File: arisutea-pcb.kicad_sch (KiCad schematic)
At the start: 51 parts, among them J12 VCC, J13 D+, J14 D-, J15 GND, J2 MISO, J3 +5V, J4 SCLK, J5 MOSI, J6 ~RES~, J7 GND, U1 USBLC6-2SC6, U2 ATMEGA32U4_QFN44, Y1 Crystal_GND24

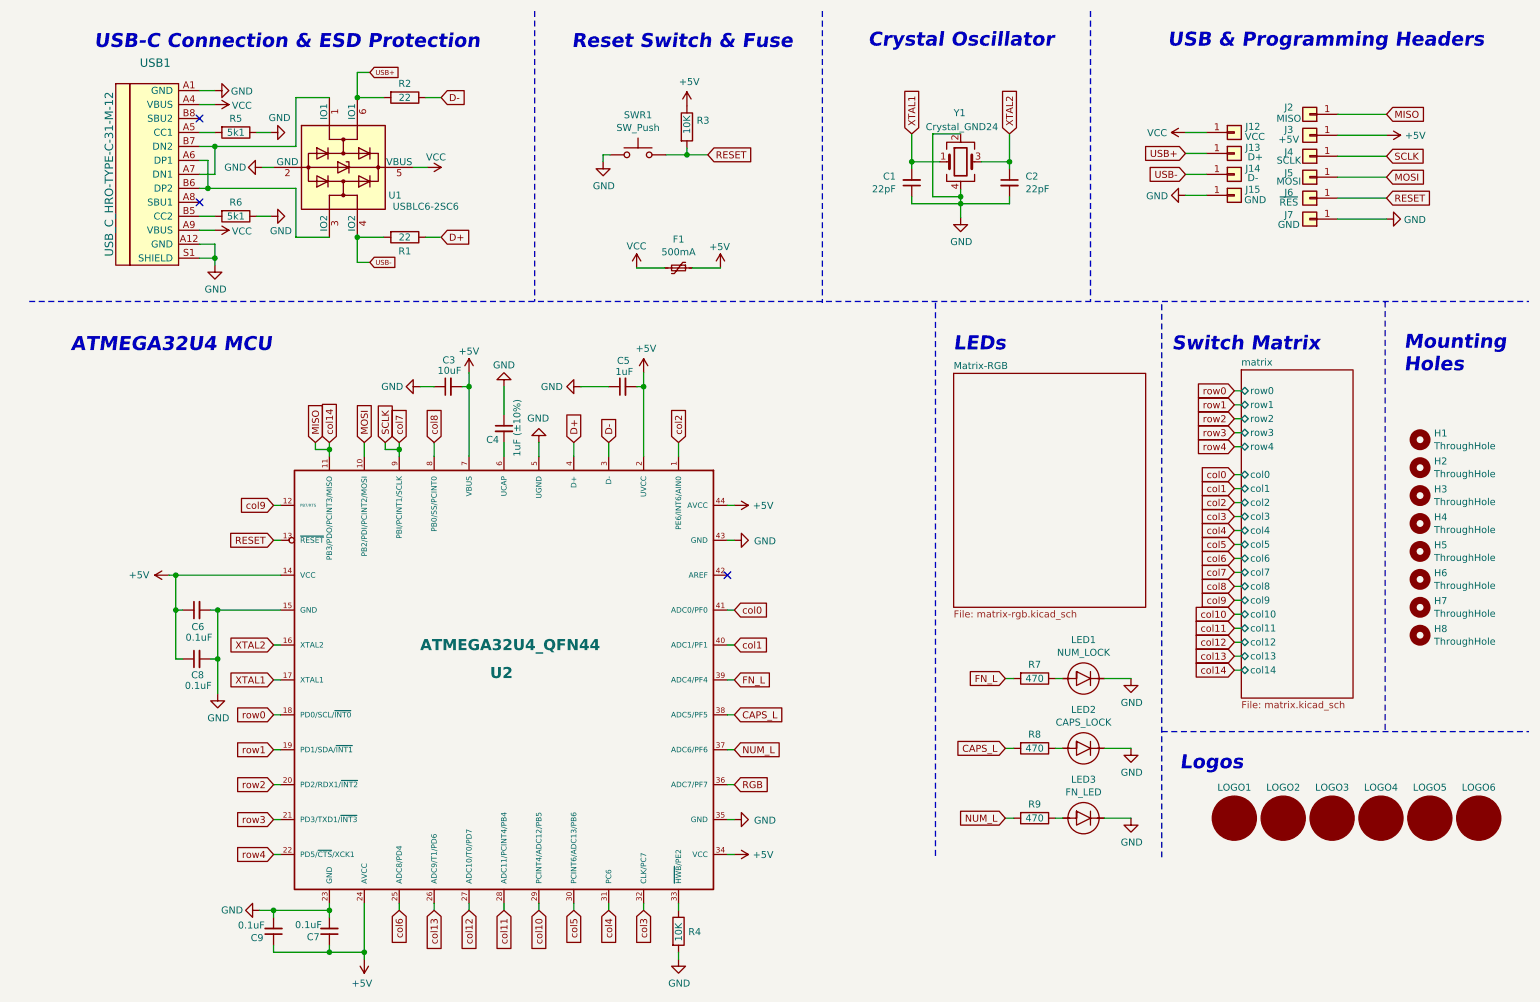
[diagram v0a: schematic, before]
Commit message: Rev 0.3
Might send this one out to get made. Not sure yet.

- Added 2 more LEDs to the edge and positioned them to be a little more evenly spread out.
- Rerouted all LED traces for better aesthetics and functionality.
- Increased power trace size. This might not be needed but it can't hurt to add with the addition of the LEDs.
- Removed programming headers. This was a personal decision as I never used them or found a need for them. It helped free up some space to route LEDs.
- Updated library, images, gerbies and BOM.
- Added a firmware that has not been tested yet, but should work in theory.
- No more position files. Too many issues at various fab houses with positions/parts/QA with previous boards.
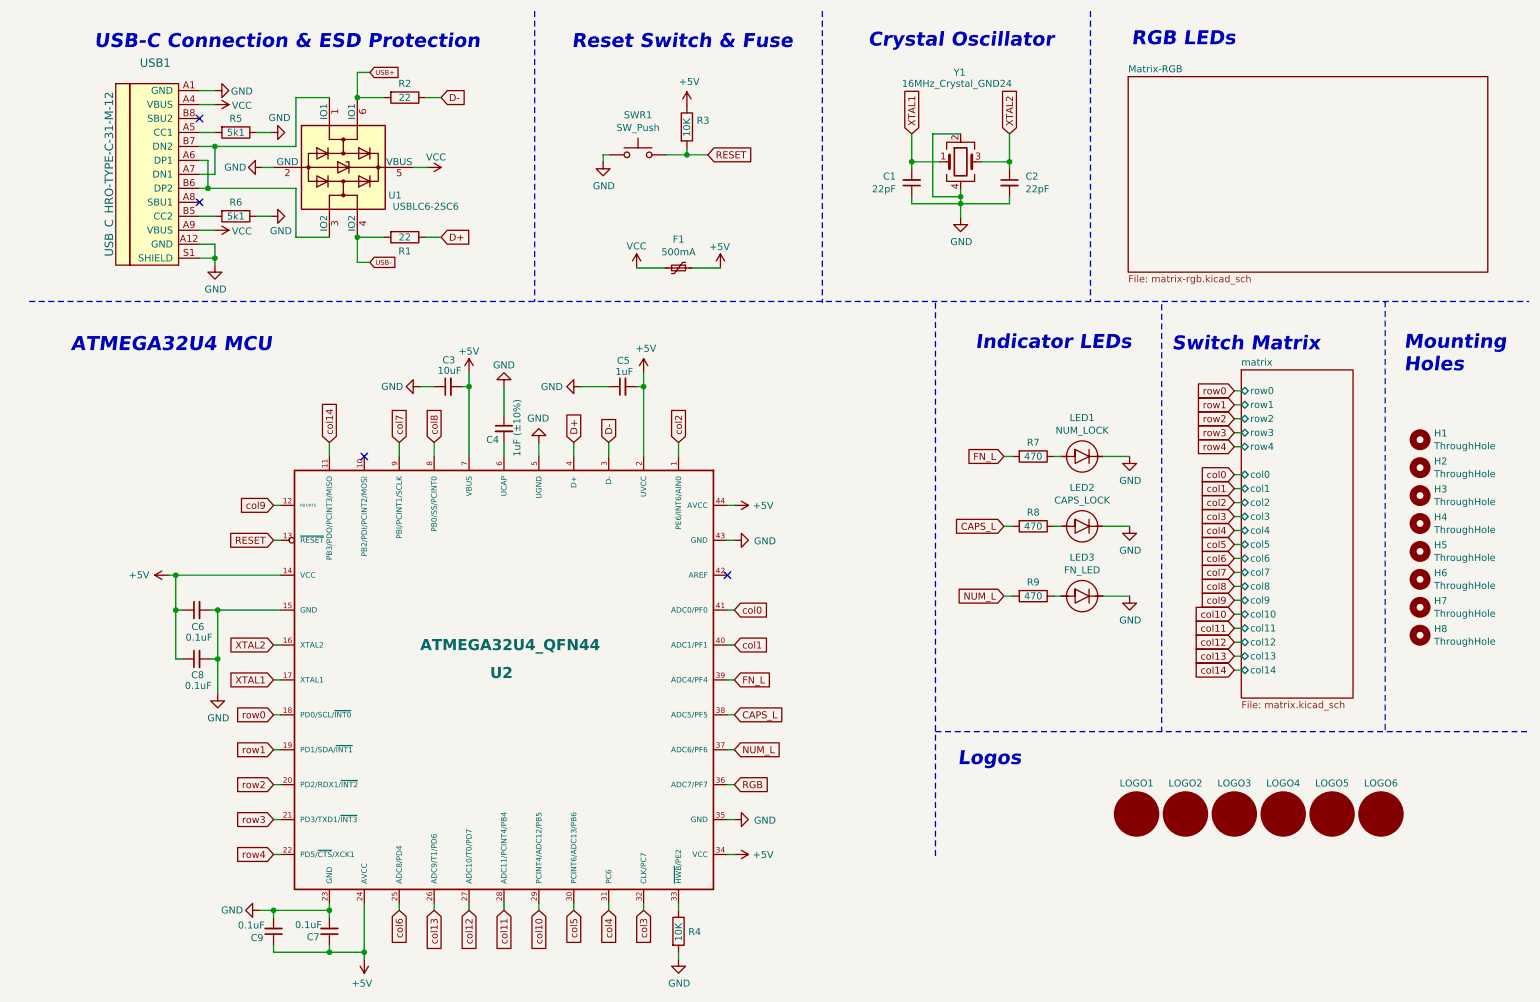
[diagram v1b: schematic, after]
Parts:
- removed J12: VCC, arisutea:PinHeader_1x01_P2.54mm_Vertical, symbol Connector_Generic:Conn_01x01
- removed J13: D+, arisutea:PinHeader_1x01_P2.54mm_Vertical, symbol Connector_Generic:Conn_01x01
- removed J14: D-, arisutea:PinHeader_1x01_P2.54mm_Vertical, symbol Connector_Generic:Conn_01x01
- removed J15, J7: GND, arisutea:PinHeader_1x01_P2.54mm_Vertical, symbol Connector_Generic:Conn_01x01
- removed J2: MISO, arisutea:PinHeader_1x01_P2.54mm_Vertical, symbol Connector_Generic:Conn_01x01
- removed J3: +5V, arisutea:PinHeader_1x01_P2.54mm_Vertical, symbol Connector_Generic:Conn_01x01
- removed J4: SCLK, arisutea:PinHeader_1x01_P2.54mm_Vertical, symbol Connector_Generic:Conn_01x01
- removed J5: MOSI, arisutea:PinHeader_1x01_P2.54mm_Vertical, symbol Connector_Generic:Conn_01x01
- removed J6: ~RES~, arisutea:PinHeader_1x01_P2.54mm_Vertical, symbol Connector_Generic:Conn_01x01
- R7, R8, R9: LCSC C27834 -> C21266
- Y1: value Crystal_GND24 -> 16MHz_Crystal_GND24
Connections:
- net MISO renamed col14
- net MOSI: no longer names the net of U2.10 (PB2/PDI/PCINT2/MOSI)
- net SCLK renamed col7
- no-connect marks 3 -> 4
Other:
- note added: "Indicator LEDs"
- note added: "RGB LEDs"
- note removed: "LEDs"
- note removed: "USB & Programming Headers"
- moved on the sheet: LED1, LED2, LED3, LOGO1, LOGO2, LOGO3, LOGO4, LOGO5, LOGO6, R7, R8, R9
